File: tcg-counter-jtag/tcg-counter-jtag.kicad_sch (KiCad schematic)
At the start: 2 parts, among them J1 MSP-FET, P1 TC2050-IDC-430

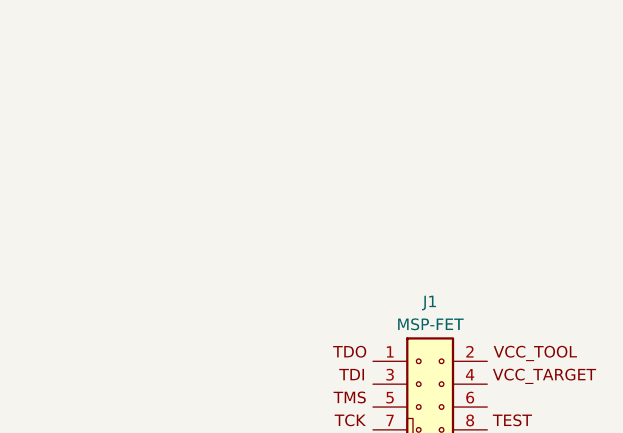
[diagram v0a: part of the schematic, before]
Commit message: Added tps72215 regulator
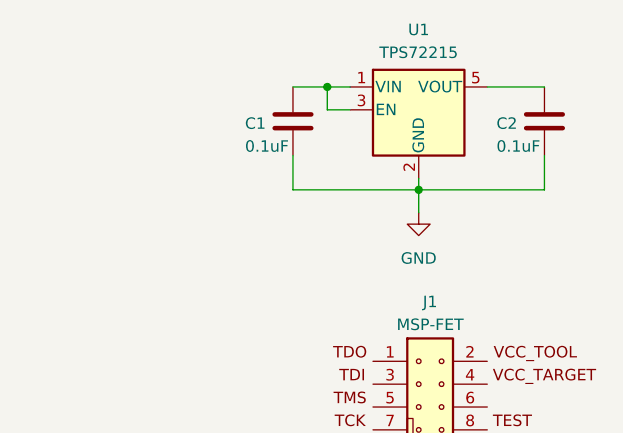
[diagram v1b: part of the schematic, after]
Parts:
- added C1, C2: 0.1uF, symbol Device:C
- added U1: TPS72215, Package_TO_SOT_SMD:SOT-23-5, symbol Regulator_Linear:TPS72215
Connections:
- new net: C1.1, U1.1 (VIN), U1.3 (EN)
- new net: C2.1, U1.5 (VOUT)
- new net GND: C1.2, C2.2, U1.2 (GND)

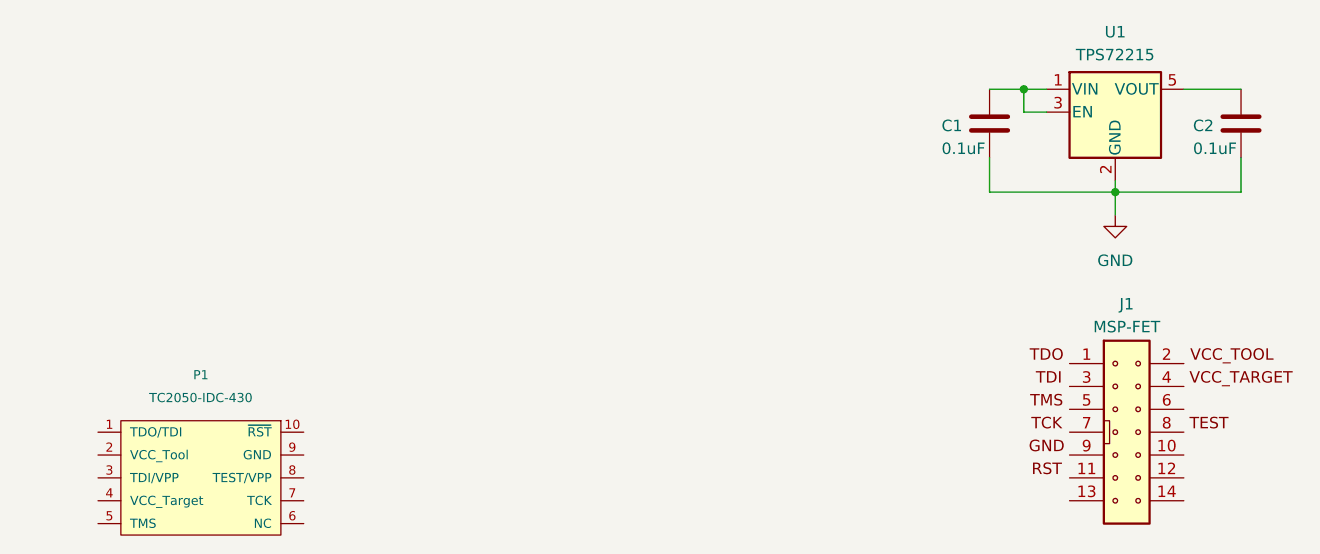
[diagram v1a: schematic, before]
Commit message: Added tag-connect header
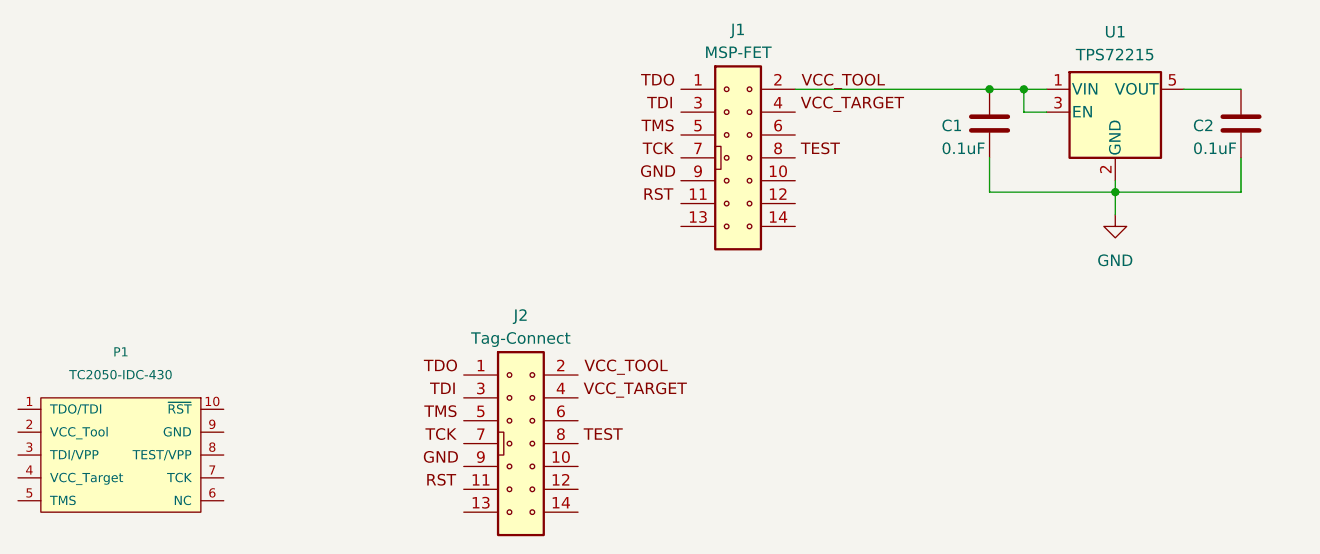
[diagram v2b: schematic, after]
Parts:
- added J2: Tag-Connect, symbol Connector_Generic:MSP-FET
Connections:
- net at C1.1, U1.1 (VIN), U1.3 (EN): now also J1.2 (VCC_TOOL)
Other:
- moved on the sheet: J1, P1
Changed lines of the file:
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@@
 	(paper "A4")
+	(junction
+		(at 168.91 40.64)
+		(diameter 0)
+		(color 0 0 0 0)
+	)
 	(junction
 		(at 172.72 40.64)
@@
 	(wire
 		(pts
+			(xy 182.88 52.07) (xy 182.88 54.61)
+		)
+		(stroke
+			(width 0)
+			(type default)
+		)
+	)
+	(wire
+		(pts
+			(xy 172.72 43.18) (xy 172.72 40.64)
+		)
+		(stroke
+			(width 0)
+			(type default)
+		)
+	)
+	(wire
+		(pts
+			(xy 168.91 48.26) (xy 168.91 52.07)
+		)
+		(stroke
+			(width 0)
+			(type default)
+		)
+	)
+	(wire
+		(pts
 			(xy 168.91 40.64) (xy 172.72 40.64)
 		)
@@
 	(wire
 		(pts
-			(xy 182.88 52.07) (xy 182.88 54.61)
-		)
-		(stroke
-			(width 0)
-			(type default)
-		)
-	)
-	(wire
-		(pts
-			(xy 172.72 43.18) (xy 172.72 40.64)
-		)
-		(stroke
-			(width 0)
-			(type default)
-		)
-	)
-	(wire
-		(pts
-			(xy 168.91 48.26) (xy 168.91 52.07)
-		)
-		(stroke
-			(width 0)
-			(type default)
-		)
-	)
-	(wire
-		(pts
 			(xy 190.5 40.64) (xy 196.85 40.64)
 		)
@@
 		(pts
 			(xy 168.91 52.07) (xy 182.88 52.07)
+		)
+		(stroke
+			(width 0)
+			(type default)
+		)
+	)
+	(wire
+		(pts
+			(xy 147.32 40.64) (xy 168.91 40.64)
 		)
 		(stroke
@@
 	(symbol
 		(lib_id "Tag-Connect:TC2050-IDC-430")
-		(at 81.28 83.82 0)
+		(at 72.39 81.28 0)
 		(unit 1)
 		(exclude_from_sim no)
@@
 		(fields_autoplaced yes)
 		(property "Reference" "P1"
-			(at 81.28 72.39 0)
+			(at 72.39 69.85 0)
 			(effects
 				(font
@@
 		)
 		(property "Value" "TC2050-IDC-430"
-			(at 81.28 74.93 0)
+			(at 72.39 72.39 0)
 			(effects
 				(font
@@
 		)
 		(property "Footprint" ""
-			(at 81.28 83.82 0)
+			(at 72.39 81.28 0)
 			(effects
 				(font
@@
 		)
 		(property "Datasheet" ""
-			(at 81.28 83.82 0)
+			(at 72.39 81.28 0)
 			(effects
 				(font
@@
 		)
 		(property "Description" ""
-			(at 81.28 83.82 0)
+			(at 72.39 81.28 0)
 			(effects
 				(font
@@
 	(symbol
 		(lib_id "Connector_Generic:MSP-FET")
-		(at 182.88 78.74 0)
+		(at 115.57 80.01 0)
+		(unit 1)
+		(exclude_from_sim no)
+		(in_bom yes)
+		(on_board yes)
+		(dnp no)
+		(property "Reference" "J2"
+			(at 116.84 65.786 0)
+			(effects
+				(font
+					(size 1.27 1.27)
+				)
+			)
+		)
+		(property "Value" "Tag-Connect"
+			(at 116.84 68.326 0)
+			(effects
+				(font
+					(size 1.27 1.27)
+				)
+			)
+		)
+		(property "Footprint" ""
+			(at 115.57 80.01 0)
+			(effects
+				(font
+					(size 1.27 1.27)
+				)
+				(hide yes)
+			)
+		)
+		(property "Datasheet" "~"
+			(at 103.632 94.996 0)
+			(effects
+				(font
+					(size 1.27 1.27)
+				)
+				(hide yes)
+			)
+		)
+		(property "Description" "Generic connector, double row, 02x07, odd/even pin numbering scheme (row 1 odd numbers, row 2 even numbers), script generated (kicad-library-utils/schlib/autogen/connector/)"
+			(at 120.65 96.012 0)
+			(effects
+				(font
+					(size 1.27 1.27)
+				)
+				(hide yes)
+			)
+		)
+		(pin "1"
+		)
+		(pin "11"
+		)
+		(pin "10"
+		)
+		(pin "12"
+		)
+		(pin "13"
+		)
+		(pin "14"
+		)
+		(pin "2"
+		)
+		(pin "3"
+		)
+		(pin "4"
+		)
+		(pin "5"
+		)
+		(pin "6"
+		)
+		(pin "7"
+		)
+		(pin "8"
+		)
+		(pin "9"
+		)
+		(instances
+			(project "tcg-counter-jtag"
+				(path "/fce5a3a6-25b7-4d59-ba24-c2c9a6bcf122"
+					(reference "J2")
+					(unit 1)
+				)
+			)
+		)
+	)
+	(symbol
+		(lib_id "Connector_Generic:MSP-FET")
+		(at 139.7 48.26 0)
 		(unit 1)
 		(exclude_from_sim no)
@@
 		(dnp no)
 		(property "Reference" "J1"
-			(at 184.15 64.516 0)
+			(at 140.97 34.036 0)
 			(effects
 				(font
@@
 		)
 		(property "Value" "MSP-FET"
-			(at 184.15 67.056 0)
+			(at 140.97 36.576 0)
 			(effects
 				(font
@@
 		)
 		(property "Footprint" ""
-			(at 182.88 78.74 0)
+			(at 139.7 48.26 0)
 			(effects
 				(font
@@
 		)
 		(property "Datasheet" "~"
-			(at 170.942 93.726 0)
+			(at 127.762 63.246 0)
 			(effects
 				(font
@@
 		)
 		(property "Description" "Generic connector, double row, 02x07, odd/even pin numbering scheme (row 1 odd numbers, row 2 even numbers), script generated (kicad-library-utils/schlib/autogen/connector/)"
-			(at 187.96 94.742 0)
-			(effects
-				(font
+			(at 144.78 64.262 0)
+			(effects
+				(font
